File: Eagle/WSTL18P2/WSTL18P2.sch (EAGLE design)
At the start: 21 parts, among them CON1 1X6CONN-1.27-ROUND, CON2 1X6CONN-1.27-ROUND, CON3 1X6CONN-1.27-ROUND, CON4 1X6CONN-1.27-ROUND, T1 ABS07AIG

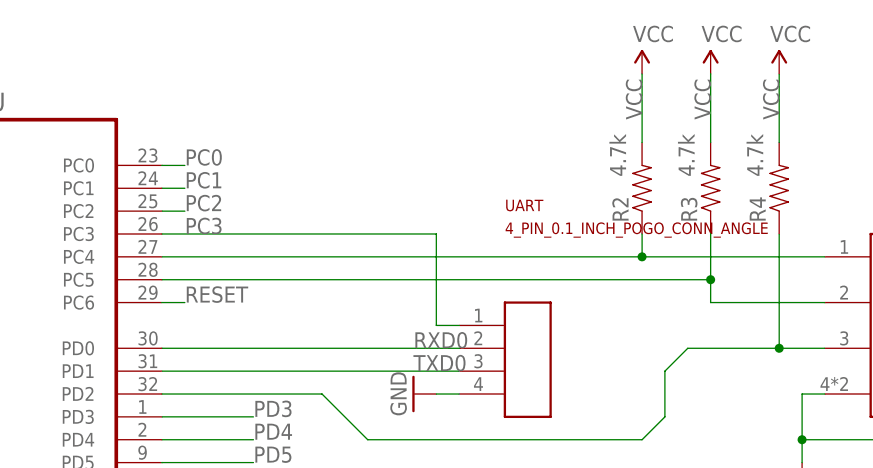
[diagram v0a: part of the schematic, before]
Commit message: Adding 1.27mm headers to TWI (I2C) lines.
This will make the TWI accessible to expansion shields.
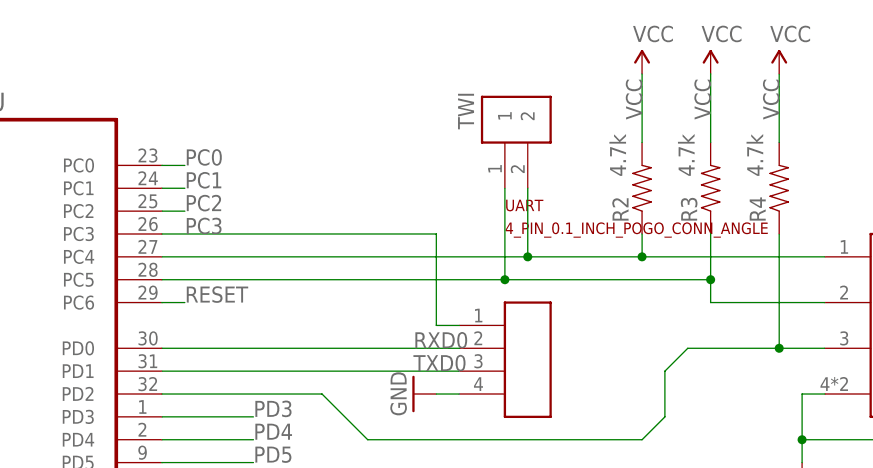
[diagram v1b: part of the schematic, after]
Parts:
- added TWI: 1X2CONN1.27, AVR_ISP_127:1X2CONN1.27
- R2, R3, R4: device Passives:RES_0402_CERAMIC -> Passives:RES_0201_CERAMIC
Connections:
- net SCL0: now also TWI.1
- net SDA0: now also TWI.2
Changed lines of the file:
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@@
 <part name="GND6" library="SparkFun-Aesthetics" deviceset="GND" device=""/>
 <part name="GND7" library="SparkFun-Aesthetics" deviceset="GND" device=""/>
-<part name="R2" library="Passives" deviceset="RES_0402_CERAMIC" device="" value="4.7k"/>
-<part name="R3" library="Passives" deviceset="RES_0402_CERAMIC" device="" value="4.7k"/>
+<part name="R2" library="Passives" deviceset="RES_0201_CERAMIC" device="" value="4.7k"/>
+<part name="R3" library="Passives" deviceset="RES_0201_CERAMIC" device="" value="4.7k"/>
 <part name="R1" library="Passives" deviceset="RES_0402_CERAMIC" device="" value="10k"/>
 <part name="LED0" library="Passives" deviceset="LED_0402" device=""/>
 <part name="GND8" library="SparkFun-Aesthetics" deviceset="GND" device=""/>
 <part name="R5" library="Passives" deviceset="RES_0402_CERAMIC" device="" value="1k"/>
-<part name="R4" library="Passives" deviceset="RES_0402_CERAMIC" device="" value="4.7k"/>
+<part name="R4" library="Passives" deviceset="RES_0201_CERAMIC" device="" value="4.7k"/>
 <part name="CON1" library="AVR_ISP_127" deviceset="1X6CONN-1.27-ROUND" device=""/>
 <part name="CON2" library="AVR_ISP_127" deviceset="1X6CONN-1.27-ROUND" device=""/>
@@
 <part name="UART" library="Connectors" deviceset="4_PIN_0.1_INCH_POGO_CONN_ANGLE" device=""/>
 <part name="U$1" library="Battery_holders" deviceset="LINX-CR2032-BAT-HLD-M-THM" device=""/>
+<part name="TWI" library="AVR_ISP_127" deviceset="1X2CONN1.27" device=""/>
 </parts>
 <sheets>
@@
 <instance part="UART" gate="G$1" x="124.46" y="48.26"/>
 <instance part="U$1" gate="G$1" x="-76.2" y="58.42"/>
+<instance part="TWI" gate="G$1" x="127" y="78.74" rot="R90"/>
 </instances>
 <busses>
@@
 <wire x1="139.7" y1="63.5" x2="139.7" y2="60.96" width="0.1524" layer="91"/>
 <pinref part="MCU" gate="A" pin="PC4"/>
-<wire x1="86.36" y1="60.96" x2="139.7" y2="60.96" width="0.1524" layer="91"/>
+<wire x1="86.36" y1="60.96" x2="127" y2="60.96" width="0.1524" layer="91"/>
 <pinref part="TMP" gate="G$1" pin="SDA"/>
+<wire x1="127" y1="60.96" x2="139.7" y2="60.96" width="0.1524" layer="91"/>
 <wire x1="139.7" y1="60.96" x2="160.02" y2="60.96" width="0.1524" layer="91"/>
 <junction x="139.7" y="60.96"/>
+<pinref part="TWI" gate="G$1" pin="2"/>
+<wire x1="127" y1="68.58" x2="127" y2="60.96" width="0.1524" layer="91"/>
+<junction x="127" y="60.96"/>
 </segment>
 </net>
@@
 <pinref part="R3" gate="G$1" pin="2"/>
 <pinref part="MCU" gate="A" pin="PC5"/>
-<wire x1="86.36" y1="58.42" x2="147.32" y2="58.42" width="0.1524" layer="91"/>
+<wire x1="86.36" y1="58.42" x2="124.46" y2="58.42" width="0.1524" layer="91"/>
 <pinref part="TMP" gate="G$1" pin="SCL"/>
+<wire x1="124.46" y1="58.42" x2="147.32" y2="58.42" width="0.1524" layer="91"/>
 <wire x1="160.02" y1="55.88" x2="147.32" y2="55.88" width="0.1524" layer="91"/>
 <wire x1="147.32" y1="58.42" x2="147.32" y2="55.88" width="0.1524" layer="91"/>
 <wire x1="147.32" y1="63.5" x2="147.32" y2="58.42" width="0.1524" layer="91"/>
 <junction x="147.32" y="58.42"/>
+<pinref part="TWI" gate="G$1" pin="1"/>
+<wire x1="124.46" y1="68.58" x2="124.46" y2="58.42" width="0.1524" layer="91"/>
+<junction x="124.46" y="58.42"/>
 </segment>
 </net>

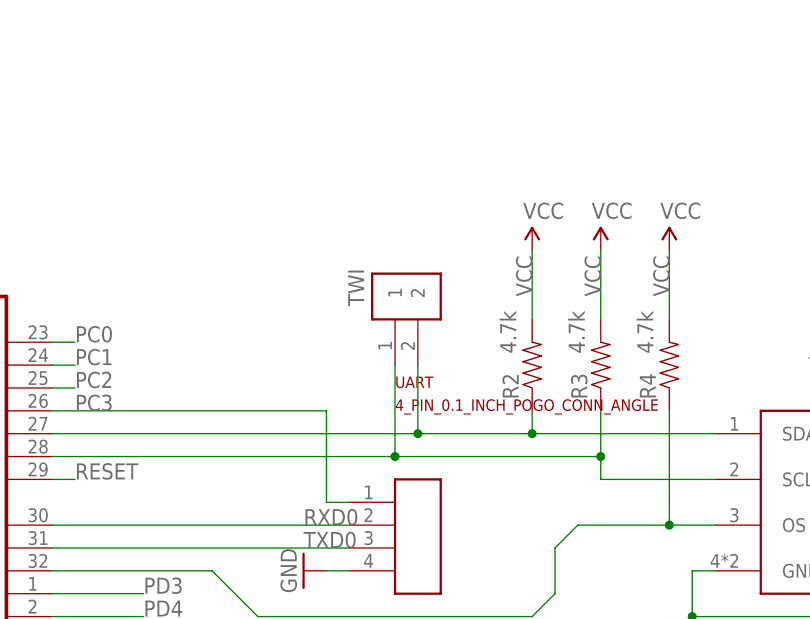
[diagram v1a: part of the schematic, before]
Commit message: Reducing signal trace widths towards 6mil
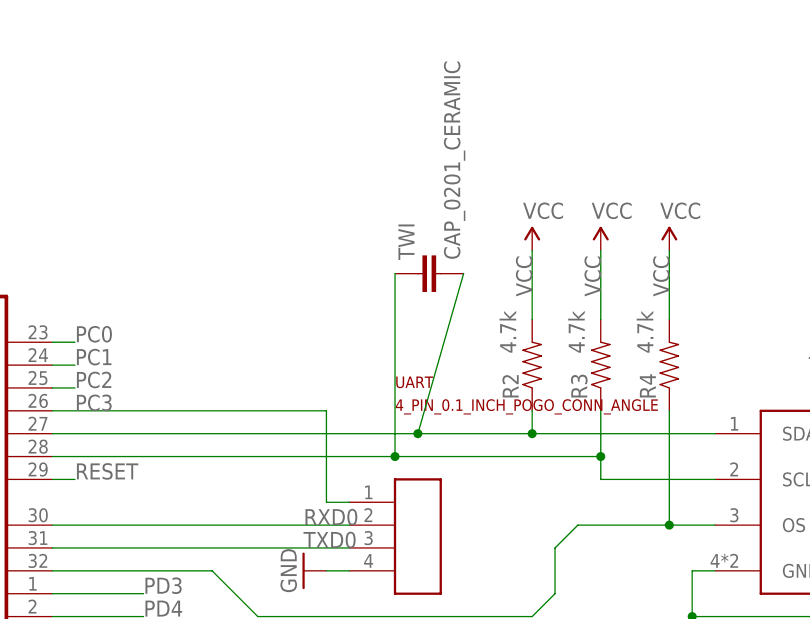
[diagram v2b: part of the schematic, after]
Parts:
- C1, C2, C3, C4, C5: device Passives:CAP_0402_CERAMIC -> Passives:CAP_0201_CERAMIC
- R1, R5: device Passives:RES_0402_CERAMIC -> Passives:RES_0201_CERAMIC
- TWI: value 1X2CONN1.27 -> CAP_0201_CERAMIC; device AVR_ISP_127:1X2CONN1.27 -> Passives:CAP_0201_CERAMIC
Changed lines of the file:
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@@
 <part name="MCU" library="ATMEGA328PB" deviceset="ATMEGA328PB" device="VQFN32"/>
 <part name="T1" library="ABS07AIG" deviceset="ABS07AIG" device=""/>
-<part name="C1" library="Passives" deviceset="CAP_0402_CERAMIC" device="" value="0.1uF"/>
-<part name="C2" library="Passives" deviceset="CAP_0402_CERAMIC" device="" value="0.1uF"/>
+<part name="C1" library="Passives" deviceset="CAP_0201_CERAMIC" device="" value="0.1uF"/>
+<part name="C2" library="Passives" deviceset="CAP_0201_CERAMIC" device="" value="0.1uF"/>
 <part name="GND27" library="SparkFun-Aesthetics" deviceset="GND" device=""/>
 <part name="GND1" library="SparkFun-Aesthetics" deviceset="GND" device=""/>
-<part name="C3" library="Passives" deviceset="CAP_0402_CERAMIC" device="" value="0.1uF"/>
+<part name="C3" library="Passives" deviceset="CAP_0201_CERAMIC" device="" value="0.1uF"/>
 <part name="GND3" library="SparkFun-Aesthetics" deviceset="GND" device=""/>
 <part name="TMP" library="MAX30205" deviceset="MAX30205" device=""/>
 <part name="GND4" library="SparkFun-Aesthetics" deviceset="GND" device=""/>
 <part name="MEM" library="Memory" deviceset="AT25DN512C-XMHF-B" device=""/>
-<part name="C4" library="Passives" deviceset="CAP_0402_CERAMIC" device="" value="0.1uF"/>
-<part name="C5" library="Passives" deviceset="CAP_0402_CERAMIC" device="" value="0.1uF"/>
+<part name="C4" library="Passives" deviceset="CAP_0201_CERAMIC" device="" value="0.1uF"/>
+<part name="C5" library="Passives" deviceset="CAP_0201_CERAMIC" device="" value="0.1uF"/>
 <part name="GND2" library="SparkFun-Aesthetics" deviceset="GND" device=""/>
 <part name="GND5" library="SparkFun-Aesthetics" deviceset="GND" device=""/>
@@
 <part name="R2" library="Passives" deviceset="RES_0201_CERAMIC" device="" value="4.7k"/>
 <part name="R3" library="Passives" deviceset="RES_0201_CERAMIC" device="" value="4.7k"/>
-<part name="R1" library="Passives" deviceset="RES_0402_CERAMIC" device="" value="10k"/>
+<part name="R1" library="Passives" deviceset="RES_0201_CERAMIC" device="" value="10k"/>
 <part name="LED0" library="Passives" deviceset="LED_0402" device=""/>
 <part name="GND8" library="SparkFun-Aesthetics" deviceset="GND" device=""/>
-<part name="R5" library="Passives" deviceset="RES_0402_CERAMIC" device="" value="1k"/>
+<part name="R5" library="Passives" deviceset="RES_0201_CERAMIC" device="" value="1k"/>
 <part name="R4" library="Passives" deviceset="RES_0201_CERAMIC" device="" value="4.7k"/>
 <part name="CON1" library="AVR_ISP_127" deviceset="1X6CONN-1.27-ROUND" device=""/>
@@
 <part name="UART" library="Connectors" deviceset="4_PIN_0.1_INCH_POGO_CONN_ANGLE" device=""/>
 <part name="U$1" library="Battery_holders" deviceset="LINX-CR2032-BAT-HLD-M-THM" device=""/>
-<part name="TWI" library="AVR_ISP_127" deviceset="1X2CONN1.27" device=""/>
+<part name="TWI" library="Passives" deviceset="CAP_0201_CERAMIC" device=""/>
 </parts>
 <sheets>
@@
 <junction x="139.7" y="60.96"/>
 <pinref part="TWI" gate="G$1" pin="2"/>
-<wire x1="127" y1="68.58" x2="127" y2="60.96" width="0.1524" layer="91"/>
+<wire x1="132.08" y1="78.74" x2="127" y2="60.96" width="0.1524" layer="91"/>
 <junction x="127" y="60.96"/>
 </segment>
@@
 <junction x="147.32" y="58.42"/>
 <pinref part="TWI" gate="G$1" pin="1"/>
-<wire x1="124.46" y1="68.58" x2="124.46" y2="58.42" width="0.1524" layer="91"/>
+<wire x1="124.46" y1="78.74" x2="124.46" y2="58.42" width="0.1524" layer="91"/>
 <junction x="124.46" y="58.42"/>
 </segment>

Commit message: Changing signal traces to 6 mil
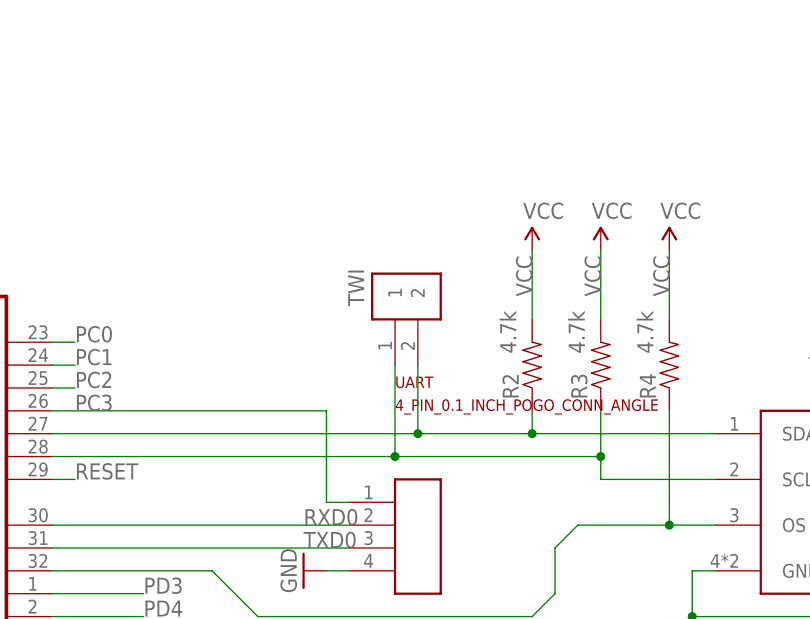
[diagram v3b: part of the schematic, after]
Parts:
- TWI: value CAP_0201_CERAMIC -> 1X2CONN1.27; device Passives:CAP_0201_CERAMIC -> AVR_ISP_127:1X2CONN1.27
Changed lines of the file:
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@@
 <part name="UART" library="Connectors" deviceset="4_PIN_0.1_INCH_POGO_CONN_ANGLE" device=""/>
 <part name="U$1" library="Battery_holders" deviceset="LINX-CR2032-BAT-HLD-M-THM" device=""/>
-<part name="TWI" library="Passives" deviceset="CAP_0201_CERAMIC" device=""/>
+<part name="TWI" library="AVR_ISP_127" deviceset="1X2CONN1.27" device=""/>
 </parts>
 <sheets>
@@
 <junction x="139.7" y="60.96"/>
 <pinref part="TWI" gate="G$1" pin="2"/>
-<wire x1="132.08" y1="78.74" x2="127" y2="60.96" width="0.1524" layer="91"/>
+<wire x1="127" y1="68.58" x2="127" y2="60.96" width="0.1524" layer="91"/>
 <junction x="127" y="60.96"/>
 </segment>
@@
 <junction x="147.32" y="58.42"/>
 <pinref part="TWI" gate="G$1" pin="1"/>
-<wire x1="124.46" y1="78.74" x2="124.46" y2="58.42" width="0.1524" layer="91"/>
+<wire x1="124.46" y1="68.58" x2="124.46" y2="58.42" width="0.1524" layer="91"/>
 <junction x="124.46" y="58.42"/>
 </segment>

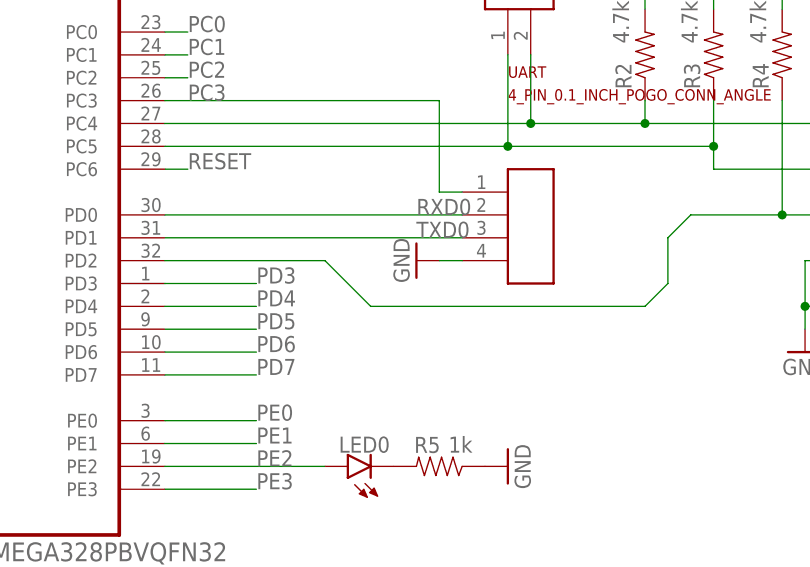
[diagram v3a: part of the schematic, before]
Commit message: More routing optimizations and changing trances to 6 mil.
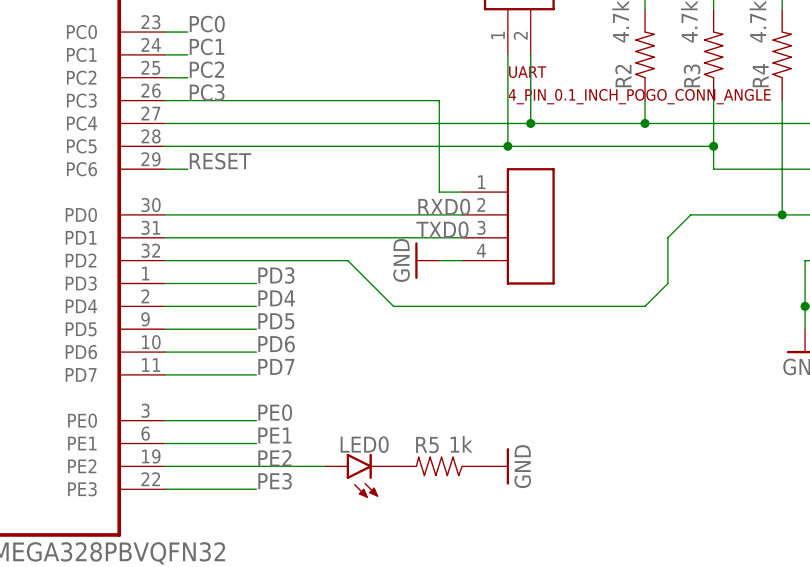
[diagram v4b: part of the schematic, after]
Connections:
- net N$3 renamed AREF
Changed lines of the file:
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@@
-</segment>
-<segment>
-<pinref part="GND11" gate="1" pin="GND"/>
-<pinref part="UART" gate="G$1" pin="4"/>
-<wire x1="116.84" y1="45.72" x2="119.38" y2="45.72" width="0.1524" layer="91"/>
 </segment>
 <segment>
@@
 <wire x1="193.04" y1="-22.86" x2="193.04" y2="-20.32" width="0.1524" layer="91"/>
 </segment>
+<segment>
+<pinref part="GND11" gate="1" pin="GND"/>
+<pinref part="UART" gate="G$1" pin="4"/>
+<wire x1="116.84" y1="45.72" x2="119.38" y2="45.72" width="0.1524" layer="91"/>
+</segment>
 </net>
-<net name="N$3" class="0">
+<net name="AREF" class="0">
 <segment>
 <pinref part="C3" gate="G$1" pin="1"/>
@@
 <pinref part="R4" gate="G$1" pin="2"/>
 <pinref part="MCU" gate="A" pin="PD2"/>
-<wire x1="86.36" y1="45.72" x2="104.14" y2="45.72" width="0.1524" layer="91"/>
-<wire x1="104.14" y1="45.72" x2="109.22" y2="40.64" width="0.1524" layer="91"/>
-<wire x1="109.22" y1="40.64" x2="139.7" y2="40.64" width="0.1524" layer="91"/>
+<wire x1="86.36" y1="45.72" x2="106.68" y2="45.72" width="0.1524" layer="91"/>
+<wire x1="106.68" y1="45.72" x2="111.76" y2="40.64" width="0.1524" layer="91"/>
+<wire x1="111.76" y1="40.64" x2="139.7" y2="40.64" width="0.1524" layer="91"/>
 <wire x1="139.7" y1="40.64" x2="142.24" y2="43.18" width="0.1524" layer="91"/>
 <pinref part="TMP" gate="G$1" pin="OS"/>
